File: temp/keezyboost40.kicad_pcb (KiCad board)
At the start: 2 copper layers, 217.6 x 68.1 mm, 92 parts, among them SW1 SW_SPST, SW10 SW_SPST, SW11 SW_SPST, SW12 SW_SPST, SW13 SW_SPST, SW14 SW_SPST, SW15 SW_SPST, SW16 SW_SPST, SW17 SW_SPST, SW18 SW_SPST, SW19 SW_SPST, SW2 SW_SPST, SW20 SW_SPST, SW21 SW_SPST, SW22 SW_SPST, SW23 SW_SPST, SW24 SW_SPST, SW25 SW_SPST, SW26 SW_SPST, SW27 SW_SPST, SW28 SW_SPST, SW29 SW_SPST, SW3 SW_SPST, SW30 SW_SPST, SW31 SW_SPST, SW32 SW_SPST, SW33 SW_SPST, SW34 SW_SPST, SW35 SW_SPST, SW36 SW_SPST, SW37 SW_SPST, SW38 SW_SPST, SW39 SW_SPST, SW4 SW_SPST, SW40 SW_SPST, SW5 SW_SPST, SW6 SW_SPST, SW7 SW_SPST, SW8 SW_SPST, SW9 SW_SPST, U1 Pico, U2 ST7735_1.8inch

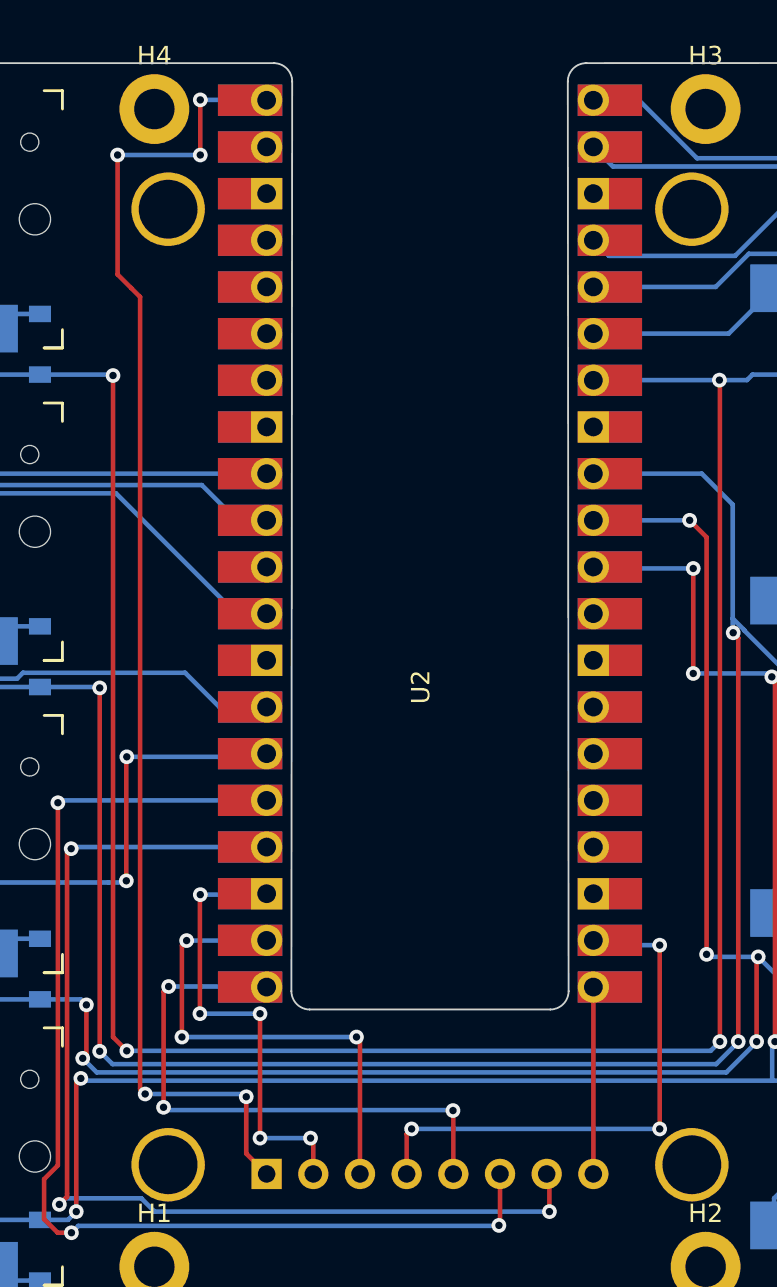
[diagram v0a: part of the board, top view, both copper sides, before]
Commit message: fixup issues with lcd interface connections
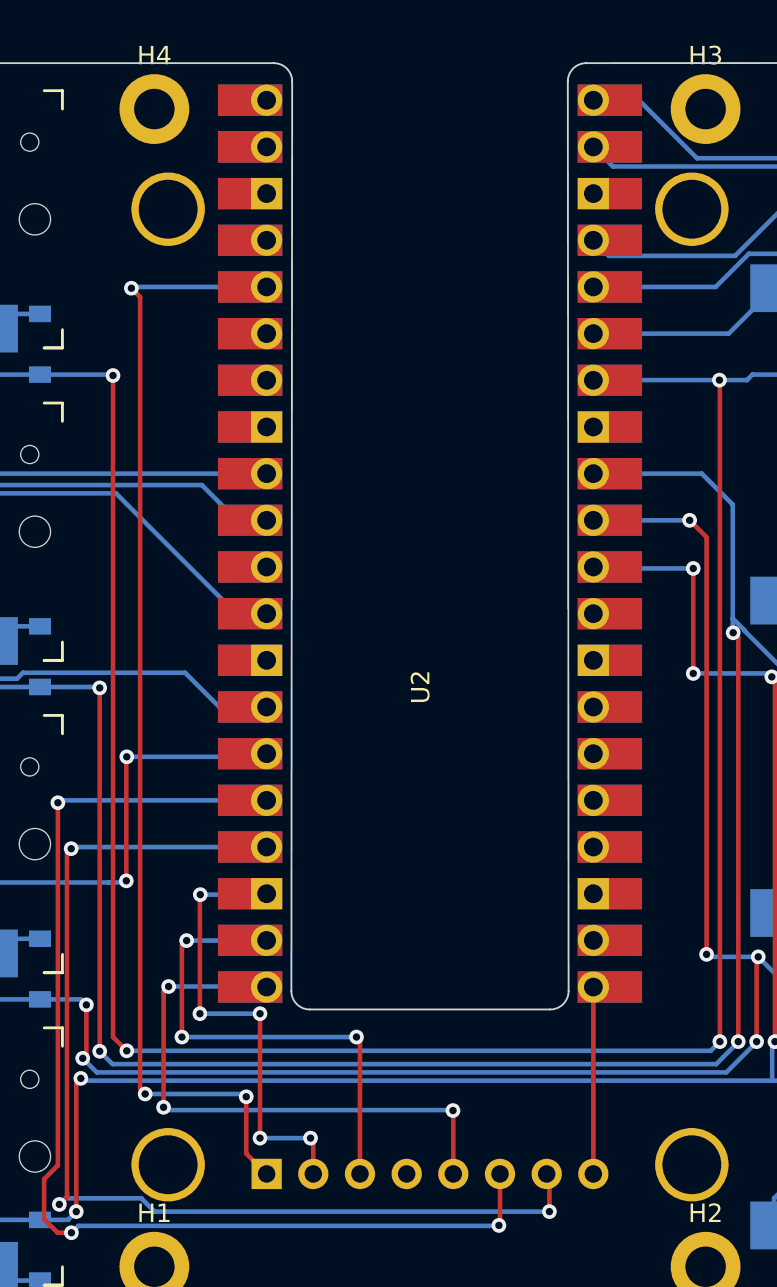
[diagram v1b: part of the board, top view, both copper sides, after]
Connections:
- net cs renamed /cs
- net dc renamed /dc
- net lcd_led renamed /lcd_led
- net sck renamed /sck
- net sda renamed /sda
- U1 pad 19: lcd_reset -> /lcd_reset
- U1 pad 36: unconnected-(U1-Pad36) -> 3v3
- U1 pad 40: vcc -> unconnected-(U1-Pad40)
- U2 pad 1: vcc -> 3v3
- U2 pad 4: lcd_reset -> /led_reset
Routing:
- net vcc: track 73.1 -> 0.00 mm, vias 5 -> 0
- net 3v3: track 0.00 -> 61.8 mm, vias 0 -> 3
- net lcd_reset: track 29.8 -> 0.00 mm, vias 3 -> 0
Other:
- board text added: "keezyboost40 v0.0"
- board text removed: "keezyboost40 v0.1"
